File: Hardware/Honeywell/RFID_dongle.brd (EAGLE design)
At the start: 53 x 38.1 mm, 13 parts, among them J1 USB_B_PTH, J5 1X2-3.5MM, J6 1X2-3.5MM, U1 4MB Flash

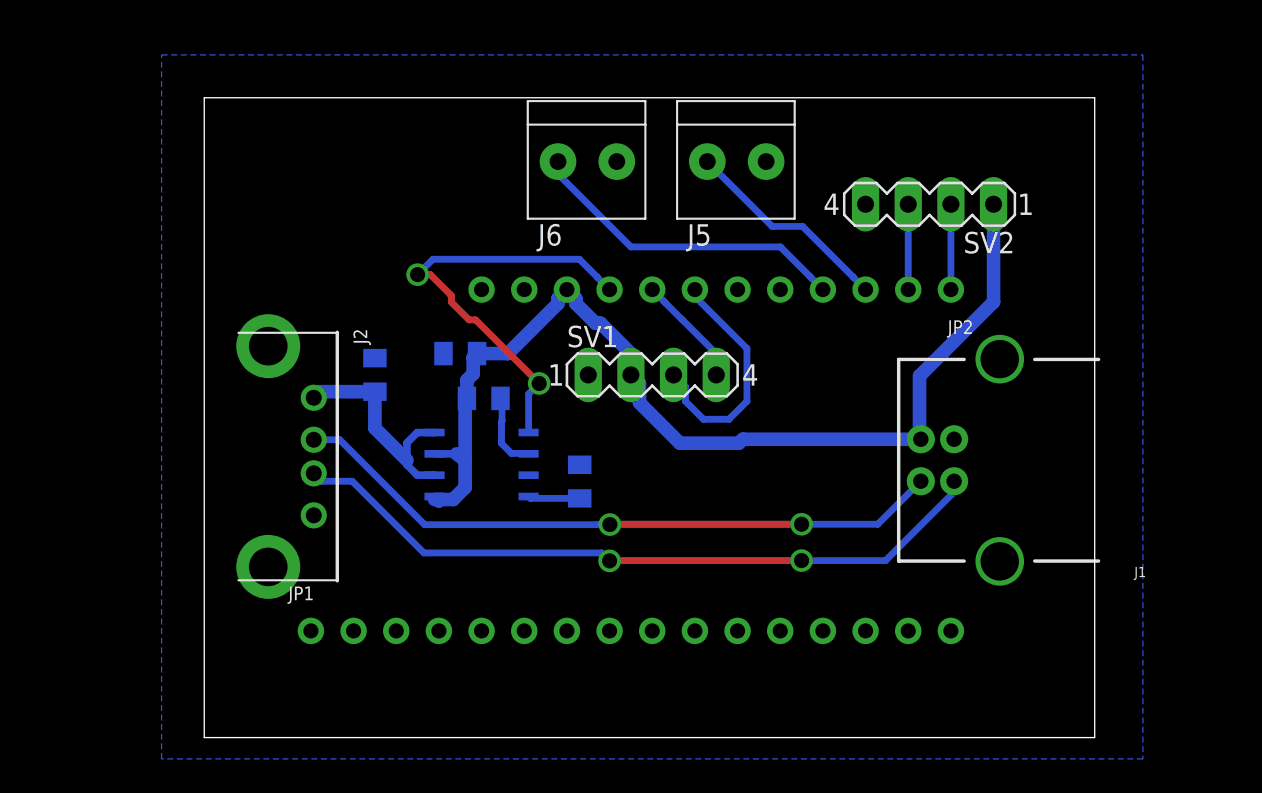
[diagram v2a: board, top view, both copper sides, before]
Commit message: HEEP-878 updated honeywell pcb for allpcb fab, swapped button GPIO
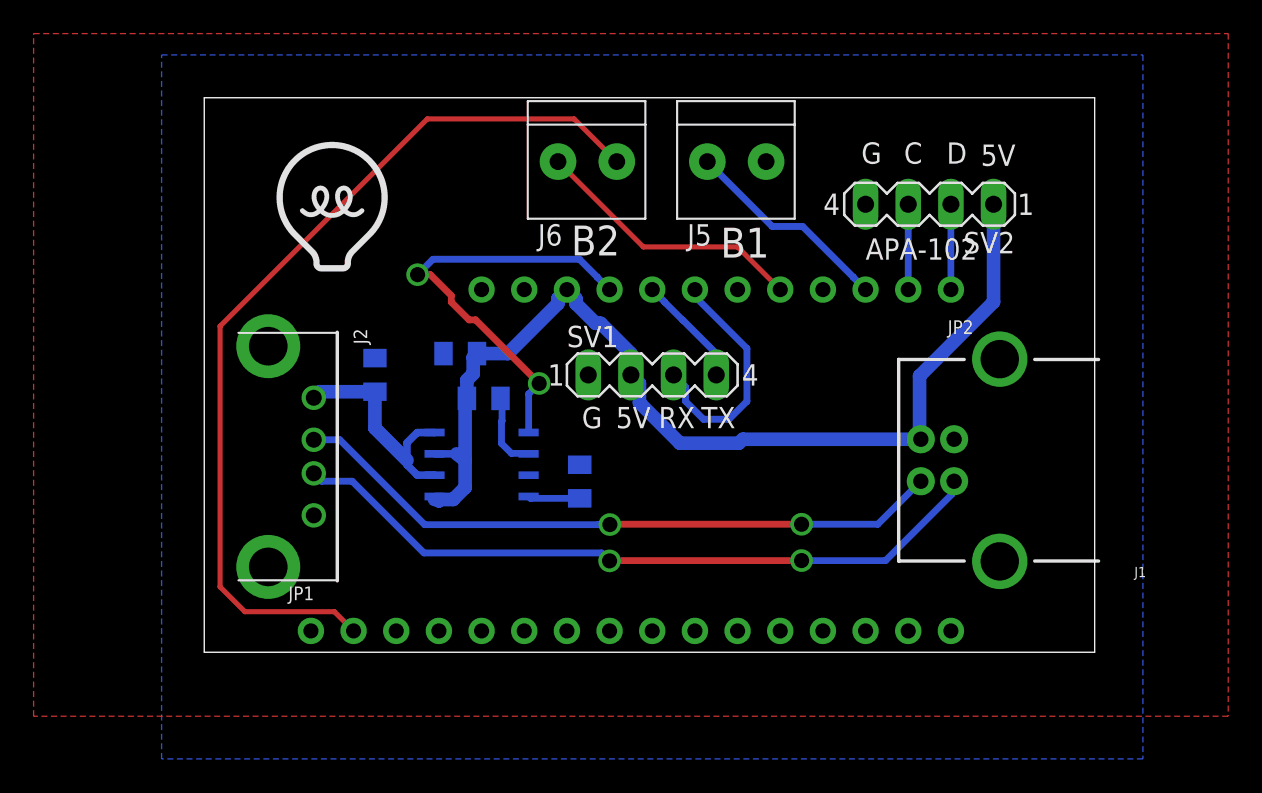
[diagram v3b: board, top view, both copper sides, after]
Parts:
- added U$1: (no value), Heep:HEEPLOGOSMALL
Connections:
- new net +3V3: J6.2, JP1.2
- net BUTT2: now also JP2.5; no longer JP2.4
- net GND: no longer J6.2
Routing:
- net +3V3: track 0.00 -> 54.4 mm
- net BUTT2: track 19.4 -> 16.4 mm
- added copper zone on layer 1, net GND
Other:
- board size 53 x 38.1 mm -> 53 x 33 mm
- board text added: "5V"
- board text added: "APA-102"
- board text added: "B1"
- board text added: "B2"
- board text added: "C"
- board text added: "D"
- board text added: "G"
- board text added: "RX"
- board text added: "TX"
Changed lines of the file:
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@@
 <board>
 <plain>
-<wire x1="0" y1="0" x2="53.01" y2="0" width="0" layer="20"/>
-<wire x1="53.01" y1="0" x2="53.01" y2="38.09" width="0" layer="20"/>
+<wire x1="0" y1="5.08" x2="53.01" y2="5.08" width="0" layer="20"/>
+<wire x1="53.01" y1="5.08" x2="53.01" y2="38.09" width="0" layer="20"/>
 <wire x1="53.01" y1="38.09" x2="0" y2="38.09" width="0" layer="20"/>
-<wire x1="0" y1="38.09" x2="0" y2="0" width="0" layer="20"/>
+<wire x1="0" y1="38.09" x2="0" y2="5.08" width="0" layer="20"/>
+<text x="30.734" y="28.575" size="1.778" layer="21">B1</text>
+<text x="21.844" y="28.702" size="1.778" layer="21">B2</text>
+<text x="22.479" y="18.415" size="1.27" layer="21">G</text>
+<text x="24.511" y="18.415" size="1.27" layer="21">5V</text>
+<text x="27.051" y="18.415" size="1.27" layer="21">RX</text>
+<text x="29.591" y="18.415" size="1.27" layer="21">TX</text>
+<text x="39.116" y="34.163" size="1.27" layer="21">G</text>
+<text x="46.228" y="34.036" size="1.27" layer="21">5V</text>
+<text x="41.656" y="34.163" size="1.27" layer="21">C</text>
+<text x="44.196" y="34.163" size="1.27" layer="21">D</text>
+<text x="39.37" y="28.448" size="1.27" layer="21">APA-102</text>
 </plain>
 <attributes>
@@
 </class>
 </classes>
-<designrules name="othermill_1_32">
+<designrules name="SeeedStudio_2layer_DRU_no_angle_20140221">
 <description language="de">&lt;b&gt;EAGLE Design Rules&lt;/b&gt;
 &lt;p&gt;
@@
 Einstellungen hier und speichern die Design Rules unter
 einem neuen Namen ab.</description>
-<description language="en">&lt;b&gt;OTHERmil 1/32&quot; End Mill design rules&lt;/b&gt;
+<description language="en">&lt;b&gt;EAGLE Design Rules&lt;/b&gt;
 &lt;p&gt;
-&lt;ul&gt;
-&lt;li&gt;Smallest drill: 32 mil&lt;/li&gt;
-&lt;li&gt;Min trace: 24mil&lt;/li&gt;
-&lt;li&gt;Min spacing: 32 mill&lt;/li&gt;
-&lt;li&gt;Dimension spacing: 10mil&lt;/li&gt;
-&lt;/ul&gt;</description>
+The default Design Rules have been set to cover
+a wide range of applications. Your particular design
+may have different requirements, so please make the
+necessary adjustments and save your customized
+design rules under a new name.</description>
+<description language="zh">&lt;b&gt;Seeed Studio EAGLE Design Rules&lt;/b&gt;
+</description>
 <param name="layerSetup" value="(1*16)"/>
-<param name="mtCopper" value="0.035mm 0.035mm 0.035mm 0.035mm 0.035mm 0.035mm 0.035mm 0.035mm 0.035mm 0.035mm 0.035mm 0.035mm 0.035mm 0.035mm 0.035mm 0.035mm"/>
-<param name="mtIsolate" value="1.5mm 0.15mm 0.2mm 0.15mm 0.2mm 0.15mm 0.2mm 0.15mm 0.2mm 0.15mm 0.2mm 0.15mm 0.2mm 0.15mm 0.2mm"/>
-<param name="mdWireWire" value="32mil"/>
-<param name="mdWirePad" value="32mil"/>
-<param name="mdWireVia" value="32mil"/>
-<param name="mdPadPad" value="32mil"/>
-<param name="mdPadVia" value="32mil"/>
-<param name="mdViaVia" value="32mil"/>
-<param name="mdSmdPad" value="8mil"/>
-<param name="mdSmdVia" value="8mil"/>
-<param name="mdSmdSmd" value="8mil"/>
+<param name="mtCopper" value="0.035mm 0.0175mm 0.035mm 0.035mm 0.035mm 0.035mm 0.035mm 0.035mm 0.035mm 0.035mm 0.035mm 0.035mm 0.035mm 0.035mm 0.0175mm 0.035mm"/>
+<param name="mtIsolate" value="1.5mm 1.1mm 0.2mm 0.15mm 0.2mm 0.15mm 0.2mm 0.15mm 0.2mm 0.15mm 0.2mm 0.15mm 0.2mm 0.15mm 0.2mm"/>
+<param name="mdWireWire" value="6mil"/>
+<param name="mdWirePad" value="6mil"/>
+<param name="mdWireVia" value="6mil"/>
+<param name="mdPadPad" value="6mil"/>
+<param name="mdPadVia" value="6mil"/>
+<param name="mdViaVia" value="6mil"/>
+<param name="mdSmdPad" value="0mil"/>
+<param name="mdSmdVia" value="0mil"/>
+<param name="mdSmdSmd" value="0mil"/>
 <param name="mdViaViaSameLayer" value="8mil"/>
 <param name="mnLayersViaInSmd" value="2"/>
 <param name="mdCopperDimension" value="10mil"/>
-<param name="mdDrill" value="8mil"/>
+<param name="mdDrill" value="10mil"/>
 <param name="mdSmdStop" value="0mil"/>
-<param name="msWidth" value="24mil"/>
-<param name="msDrill" value="31mil"/>
-<param name="msMicroVia" value="9.99mm"/>
+<param name="msWidth" value="6mil"/>
+<param name="msDrill" value="12mil"/>
+<param name="msMicroVia" value="12mil"/>
 <param name="msBlindViaRatio" value="0.5"/>
 <param name="rvPadTop" value="0.25"/>
@@
 <param name="rvMicroViaOuter" value="0.25"/>
 <param name="rvMicroViaInner" value="0.25"/>
-<param name="rlMinPadTop" value="12mil"/>
-<param name="rlMaxPadTop" value="12mil"/>
+<param name="rlMinPadTop" value="10mil"/>
+<param name="rlMaxPadTop" value="20mil"/>
 <param name="rlMinPadInner" value="10mil"/>
 <param name="rlMaxPadInner" value="20mil"/>
-<param name="rlMinPadBottom" value="12mil"/>
-<param name="rlMaxPadBottom" value="12mil"/>
-<param name="rlMinViaOuter" value="8mil"/>
+<param name="rlMinPadBottom" value="10mil"/>
+<param name="rlMaxPadBottom" value="20mil"/>
+<param name="rlMinViaOuter" value="6mil"/>
 <param name="rlMaxViaOuter" value="20mil"/>
-<param name="rlMinViaInner" value="8mil"/>
+<param name="rlMinViaInner" value="6mil"/>
 <param name="rlMaxViaInner" value="20mil"/>
 <param name="rlMinMicroViaOuter" value="4mil"/>
@@
 <param name="psTop" value="-1"/>
 <param name="psBottom" value="-1"/>
-<param name="psFirst" value="-1"/>
+<param name="psFirst" value="0"/>
 <param name="psElongationLong" value="100"/>
 <param name="psElongationOffset" value="100"/>
@@
 <param name="mlMinCreamFrame" value="0mil"/>
 <param name="mlMaxCreamFrame" value="0mil"/>
-<param name="mlViaStopLimit" value="20mil"/>
+<param name="mlViaStopLimit" value="100mil"/>
 <param name="srRoundness" value="0"/>
 <param name="srMinRoundness" value="0mil"/>
@@
 <param name="checkAngle" value="0"/>
 <param name="checkFont" value="1"/>
-<param name="checkRestrict" value="1"/>
+<param name="checkRestrict" value="0"/>
 <param name="checkStop" value="0"/>
 <param name="checkValues" value="0"/>
@@
 <element name="R1" library="adafruit" library_urn="urn:adsk.eagle:library:420" package="R0805" value="100K" x="16.637" y="20.193" rot="MR180"/>
 <element name="R2" library="adafruit" library_urn="urn:adsk.eagle:library:420" package="R0805" value="4.7K" x="22.352" y="15.24" rot="MR90"/>
+<element name="U$1" library="Heep" package="HEEPLOGOSMALL" value="" x="7.62" y="31.75"/>
 </elements>
 <signals>
@@
 <contactref element="J1" pad="GND"/>
 <contactref element="J5" pad="2"/>
-<contactref element="J6" pad="2"/>
 <contactref element="SV1" pad="1"/>
 <contactref element="SV2" pad="4"/>
@@
 <contactref element="J2" pad="S1"/>
 <contactref element="J2" pad="S2"/>
+<polygon width="0.3048" layer="1">
+<vertex x="-10.16" y="41.91"/>
+<vertex x="60.96" y="41.91"/>
+<vertex x="60.96" y="1.27"/>
+<vertex x="-10.16" y="1.27"/>
+</polygon>
 </signal>
 <signal name="EN1">
@@
 <signal name="BUTT2">
 <contactref element="J6" pad="1"/>
-<contactref element="JP2" pad="4"/>
-<wire x1="36.83" y1="26.67" x2="36.0934" y2="27.4066" width="0.4064" layer="16"/>
-<wire x1="36.0934" y1="27.4066" x2="36.0934" y2="27.41699375" width="0.4064" layer="16"/>
-<wire x1="36.0934" y1="27.41699375" x2="34.30039375" y2="29.21" width="0.4064" layer="16"/>
-<wire x1="34.30039375" y1="29.21" x2="25.4" y2="29.21" width="0.4064" layer="16"/>
-<wire x1="25.4" y1="29.21" x2="21.06" y2="33.55" width="0.4064" layer="16"/>
-<wire x1="21.06" y1="33.55" x2="21.06" y2="34.29" width="0.4064" layer="16"/>
+<contactref element="JP2" pad="5"/>
+<wire x1="21.06" y1="34.29" x2="26.14" y2="29.21" width="0.3048" layer="1"/>
+<wire x1="31.75" y1="29.21" x2="34.29" y2="26.67" width="0.3048" layer="1"/>
+<wire x1="26.14" y1="29.21" x2="31.75" y2="29.21" width="0.3048" layer="1"/>
 </signal>
 <signal name="APA_DATA">
@@
 <wire x1="19.421" y1="14.24" x2="19.31" y2="14.351" width="0.4064" layer="16"/>
 </signal>
+<signal name="+3V3">
+<contactref element="J6" pad="2"/>
+<contactref element="JP1" pad="2"/>
+<wire x1="24.56" y1="34.29" x2="22.02" y2="36.83" width="0.3048" layer="1"/>
+<wire x1="0.9398" y1="24.48888125" x2="0.9398" y2="8.97111875" width="0.3048" layer="1"/>
+<wire x1="13.28091875" y1="36.83" x2="0.9398" y2="24.48888125" width="0.3048" layer="1"/>
+<wire x1="22.02" y1="36.83" x2="13.28091875" y2="36.83" width="0.3048" layer="1"/>
+<wire x1="8.82855625" y1="6.35" x2="8.89" y2="6.35" width="0.3048" layer="1"/>
+<wire x1="0.9398" y1="8.97111875" x2="2.41791875" y2="7.493" width="0.3048" layer="1"/>
+<wire x1="7.747" y1="7.493" x2="8.89" y2="6.35" width="0.3048" layer="1"/>
+<wire x1="2.41791875" y1="7.493" x2="7.747" y2="7.493" width="0.3048" layer="1"/>
+</signal>
 </signals>
